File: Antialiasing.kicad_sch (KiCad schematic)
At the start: 3 parts

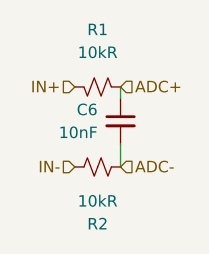
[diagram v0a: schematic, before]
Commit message: Updated to use resistor arrays
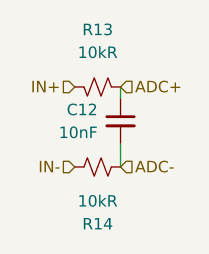
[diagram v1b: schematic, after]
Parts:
- renumbered C6 to C12, R1 to R13, R2 to R14
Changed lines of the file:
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@@
 		(on_board yes)
 		(dnp no)
-		(property "Reference" "R2"
+		(property "Reference" "R14"
 			(at 154.94 114.3 90)
 			(effects
@@
 		(dnp no)
 		(fields_autoplaced yes)
-		(property "Reference" "C6"
+		(property "Reference" "C12"
 			(at 154.94 101.6062 0)
 			(effects
@@
 		(dnp no)
 		(fields_autoplaced yes)
-		(property "Reference" "R1"
+		(property "Reference" "R13"
 			(at 154.94 92.71 90)
 			(effects
